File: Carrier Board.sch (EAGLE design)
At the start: 54 parts, among them J1 H4P-SMD-2.0, J2 H4P-SMD-2.0, J4 S2B-PH-SM4-TB(LF)(SN), J5 S2B-PH-SM4-TB(LF)(SN), Q1 MMBT2222A, SW2 MF-SW-TACT-6MM, U1 TMP36GRTZ, U2 TPL5010, U3 MB85RC64, U7 NAND

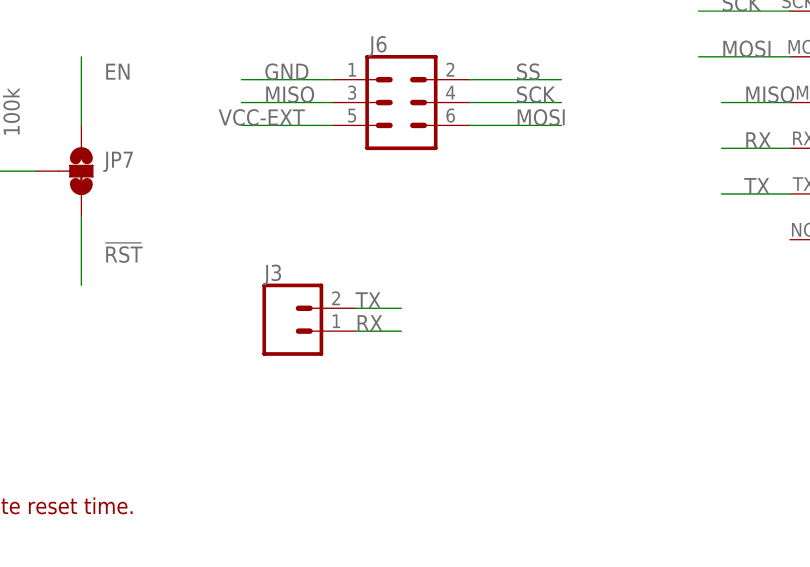
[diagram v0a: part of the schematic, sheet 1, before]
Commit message: v1.1 - Added a GND pin to serial
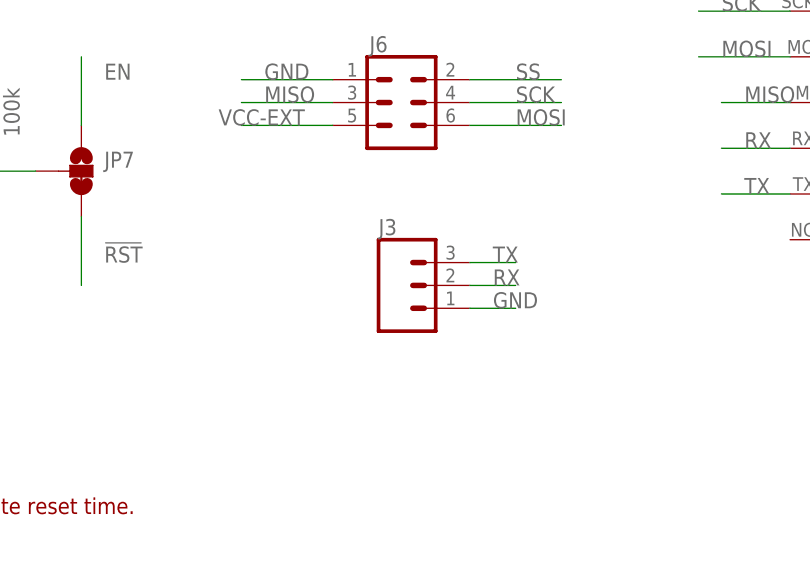
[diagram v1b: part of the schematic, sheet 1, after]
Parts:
- J3: device SparkFun-Connectors:CONN_02 -> SparkFun-Connectors:CONN_03LOCK
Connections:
- net GND: now also J3.1
- net RX: now also J3.2; no longer J3.1
- net TX: now also J3.3; no longer J3.2
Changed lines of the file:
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@@
 <part name="JP4" library="SparkFun" deviceset="STAND-OFF" device=""/>
 <part name="JP6" library="SparkFun" deviceset="STAND-OFF" device=""/>
-<part name="J3" library="SparkFun-Connectors" deviceset="CONN_02" device=""/>
 <part name="J5" library="SparkFun-Connectors" deviceset="JST_2MM_MALE" device="" value="S2B-PH-SM4-TB(LF)(SN)">
 <attribute name="MFG" value="S2B-PH-SM4-TB(LF)(SN)"/>
@@
 <part name="GND8" library="supply1" library_urn="urn:adsk.eagle:library:371" deviceset="GND" device=""/>
 <part name="J6" library="SparkFun-Connectors" library_urn="urn:adsk.eagle:library:513" deviceset="CONN_03X2" device="2X3_SILK_MALE_PTH" package3d_urn="urn:adsk.eagle:package:38016/1"/>
+<part name="J3" library="SparkFun-Connectors" library_urn="urn:adsk.eagle:library:513" deviceset="CONN_03" device="LOCK" package3d_urn="urn:adsk.eagle:package:38071/1"/>
 </parts>
 <sheets>
@@
 <instance part="JP4" gate="G$1" x="233.68" y="17.78" smashed="yes"/>
 <instance part="JP6" gate="G$1" x="243.84" y="17.78" smashed="yes"/>
-<instance part="J3" gate="G$1" x="101.6" y="81.28" smashed="yes">
-<attribute name="VALUE" x="99.06" y="76.454" size="1.778" layer="96" font="vector"/>
-<attribute name="NAME" x="99.06" y="86.868" size="1.778" layer="95" font="vector"/>
-</instance>
 <instance part="R3" gate="G$1" x="68.58" y="106.68" smashed="yes" rot="R90">
 <attribute name="NAME" x="67.0814" y="102.87" size="1.778" layer="95" rot="R90"/>
@@
 <attribute name="NAME" x="110.744" y="112.268" size="1.778" layer="95" font="vector"/>
 <attribute name="VALUE" x="110.998" y="100.838" size="1.778" layer="96" font="vector" align="top-left"/>
+</instance>
+<instance part="J3" gate="J$1" x="114.3" y="86.36" smashed="yes">
+<attribute name="VALUE" x="111.76" y="78.994" size="1.778" layer="96" font="vector"/>
+<attribute name="NAME" x="111.76" y="91.948" size="1.778" layer="95" font="vector"/>
 </instance>
 </instances>
@@
 <label x="99.06" y="109.22" size="1.778" layer="95"/>
 </segment>
+<segment>
+<wire x1="127" y1="83.82" x2="121.92" y2="83.82" width="0.1524" layer="91"/>
+<pinref part="J3" gate="J$1" pin="1"/>
+<label x="124.46" y="83.82" size="1.778" layer="95"/>
+</segment>
 </net>
 <net name="SCL" class="0">
@@
 <net name="TX" class="0">
 <segment>
-<pinref part="J3" gate="G$1" pin="2"/>
-<wire x1="109.22" y1="83.82" x2="114.3" y2="83.82" width="0.1524" layer="91"/>
-<label x="109.22" y="83.82" size="1.778" layer="95"/>
-</segment>
-<segment>
 <pinref part="BORON/ARGON/XENON" gate="G$1" pin="TX"/>
 <wire x1="157.48" y1="96.52" x2="149.86" y2="96.52" width="0.1524" layer="91"/>
 <label x="152.4" y="96.52" size="1.778" layer="95"/>
+</segment>
+<segment>
+<wire x1="121.92" y1="88.9" x2="127" y2="88.9" width="0.1524" layer="91"/>
+<pinref part="J3" gate="J$1" pin="3"/>
+<label x="124.46" y="88.9" size="1.778" layer="95"/>
 </segment>
 </net>
@@
 <net name="RX" class="0">
 <segment>
-<pinref part="J3" gate="G$1" pin="1"/>
-<wire x1="109.22" y1="81.28" x2="114.3" y2="81.28" width="0.1524" layer="91"/>
-<label x="109.22" y="81.28" size="1.778" layer="95"/>
-</segment>
-<segment>
 <pinref part="BORON/ARGON/XENON" gate="G$1" pin="RX"/>
 <wire x1="157.48" y1="101.6" x2="149.86" y2="101.6" width="0.1524" layer="91"/>
 <label x="152.4" y="101.6" size="1.778" layer="95"/>
 </segment>
-</net>
+<segment>
+<wire x1="121.92" y1="86.36" x2="127" y2="86.36" width="0.1524" layer="91"/>
+<pinref part="J3" gate="J$1" pin="2"/>
+<label x="124.46" y="86.36" size="1.778" layer="95"/>
+</segment>
+</net>

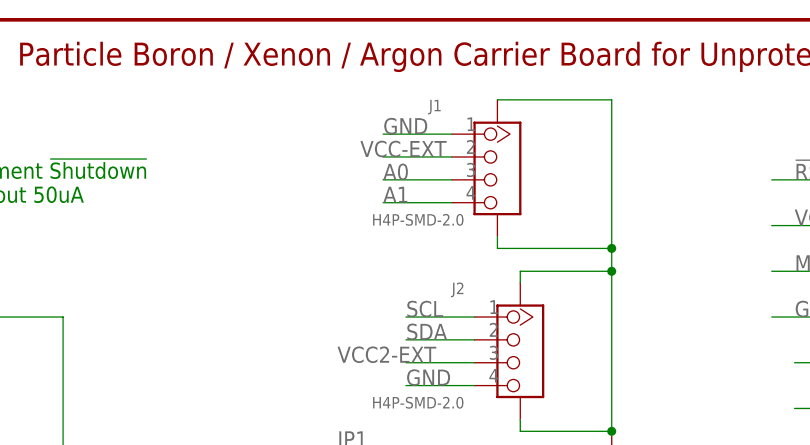
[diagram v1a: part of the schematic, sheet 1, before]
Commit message: Fixed Analoge Header Pins
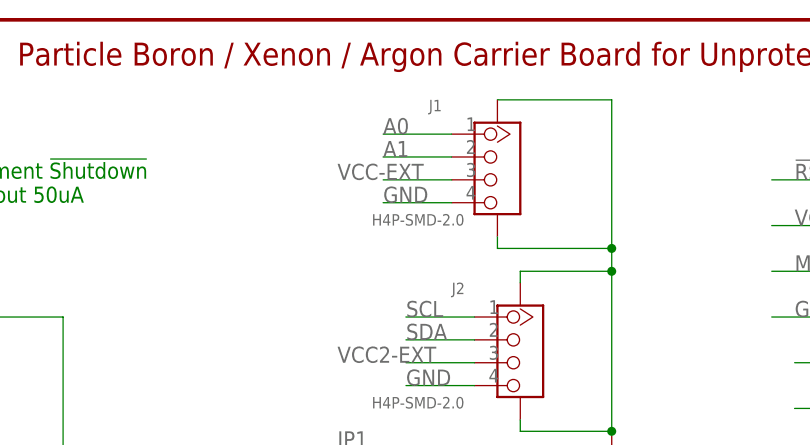
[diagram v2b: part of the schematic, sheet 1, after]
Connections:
- net A0: now also J1.1; no longer J1.3
- net A1: now also J1.2; no longer J1.4
- net GND: now also J1.4; no longer J1.1
- net VCC-EXT: now also J1.3; no longer J1.2
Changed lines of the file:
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@@
-</segment>
-<segment>
-<wire x1="104.14" y1="172.72" x2="111.76" y2="172.72" width="0.1524" layer="91"/>
-<label x="104.14" y="172.72" size="1.778" layer="95"/>
-<pinref part="J1" gate="G$1" pin="1"/>
 </segment>
 <segment>
@@
 <label x="124.46" y="83.82" size="1.778" layer="95"/>
 </segment>
+<segment>
+<wire x1="104.14" y1="165.1" x2="111.76" y2="165.1" width="0.1524" layer="91"/>
+<pinref part="J1" gate="G$1" pin="4"/>
+<label x="104.14" y="165.1" size="1.778" layer="95"/>
+</segment>
 </net>
 <net name="SCL" class="0">
@@
 <net name="VCC-EXT" class="0">
 <segment>
-<wire x1="104.14" y1="170.18" x2="111.76" y2="170.18" width="0.1524" layer="91"/>
-<pinref part="J1" gate="G$1" pin="2"/>
-<label x="101.6" y="170.18" size="1.778" layer="95"/>
-</segment>
-<segment>
 <pinref part="J6" gate="G$1" pin="5"/>
 <wire x1="106.68" y1="104.14" x2="96.52" y2="104.14" width="0.1524" layer="91"/>
 <label x="93.98" y="104.14" size="1.778" layer="95"/>
+</segment>
+<segment>
+<wire x1="104.14" y1="167.64" x2="111.76" y2="167.64" width="0.1524" layer="91"/>
+<pinref part="J1" gate="G$1" pin="3"/>
+<label x="99.06" y="167.64" size="1.778" layer="95"/>
 </segment>
 </net>
@@
 </segment>
 <segment>
-<wire x1="104.14" y1="167.64" x2="111.76" y2="167.64" width="0.1524" layer="91"/>
-<label x="104.14" y="167.64" size="1.778" layer="95"/>
-<pinref part="J1" gate="G$1" pin="3"/>
+<pinref part="J1" gate="G$1" pin="1"/>
+<wire x1="111.76" y1="172.72" x2="104.14" y2="172.72" width="0.1524" layer="91"/>
+<label x="104.14" y="172.72" size="1.778" layer="95"/>
 </segment>
 </net>
@@
 </segment>
 <segment>
-<wire x1="104.14" y1="165.1" x2="111.76" y2="165.1" width="0.1524" layer="91"/>
-<label x="104.14" y="165.1" size="1.778" layer="95"/>
-<pinref part="J1" gate="G$1" pin="4"/>
-</segment>
-</net>
+<pinref part="J1" gate="G$1" pin="2"/>
+<wire x1="111.76" y1="170.18" x2="104.14" y2="170.18" width="0.1524" layer="91"/>
+<label x="104.14" y="170.18" size="1.778" layer="95"/>
+</segment>
+</net>

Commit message: Next major revision - Added RTC
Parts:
- removed BORON/ARGON/XENON: PARTICLE-DEVICES-BORON, Carrier Board:PARTICLE-DEVICES-BORON
- removed D3: MF-DIO-SOD123-BAT42, MF_Discrete_Semiconductor:DIODES_BAT42_SOD-123
- removed JP7: JUMPER-SMT_3_1-NC_TRACE_SILK, SparkFun-Jumpers:JUMPER-SMT_3_1-NC_TRACE_SILK
- removed JP9: JUMPER-SMT_2_NC_PASTE_SILK, SparkFun-Jumpers:JUMPER-SMT_2_NC_PASTE_SILK
- removed R10: 10k, SparkFun-Passives:RESISTOR0805-RES
- removed R11, R13, R14: 100k, SparkFun-Passives:RESISTOR0805-RES
- removed R12: 100, SparkFun-Passives:RESISTOR0805-RES
- removed S2: B3F-4000, adafruit:40-XX-ROUND
- removed SW2: MF-SW-TACT-6MM, MF_Switches:TACT_6MM
- added C11: 10pF, SparkFun-Capacitors:CAP0805
- added C12: 8.2pF, SparkFun-Capacitors:CAP0805
- added C6, C7: 0.1uF, SparkFun-Capacitors:CAP0805
- added H1, H2, H3, H4: STAND-OFF-M2.5, Custom Components:STAND-OFF-M2.5
- added JP2: (no value), SparkFun-Connectors:M06LOCK
- added P1: PARTICLE-DEVICES-BORON, Carrier Board:PARTICLE-DEVICES-BORON
- added Q2: BSS138, transistor-small-signal:BSS123
- added R20, R21, R22: 10k, SparkFun-Passives:RESISTOR0805-RES
- added R8, R9: 100, SparkFun-Passives:RESISTOR0805-RES
- added S1: (no value), SparkFun-Switches:SWITCH-SPDT-SMD-AYZ0202
- added SW1: MF-SW-TACT-6MM, MF_Switches:TACT_6MM
- added U4, U5: TPS22810, Custom Components:TPS22810
- added U8: MCP79410T-I/SN, Custom Components:MCP79410T-I/SN
- added Y1: ECS-.327-6-17X-TR, Custom Components:ECS-.327-6-17X-TR
- C1: HOUSEPART (none) -> YES; MPN (none) -> MF-CAP-0805-0.1uF; POPULATE (none) -> 1
- C2: MPN (none) -> MF-CAP-0805-1uF
- C3: MPN (none) -> MF-CAP-0805-0.1uF; POPULATE (none) -> 1
- C4: value 0.1uF -> 10nF; HOUSEPART (none) -> No; MPN (none) -> 08051C103K4T2A; POPULATE (none) -> 1
- C5: value 1uF -> 10nF; HOUSEPART (none) -> No; MPN (none) -> 08051C103K4T2A; POPULATE (none) -> 1
- C8: HOUSEPART (none) -> 1; MPN (none) -> MF-CAP-10MM-470uF
- D1, D2: value MF-DIO-SOD123-BAT42 -> BAT42
- F1: value 1.5A - SLOW BLOW -> 6V/0.5A; MPN (none) -> 046801.5NR
- F2, F3: value 500mA - FAST BLOW -> 6V/0.5A; MPN (none) -> 0466.500NR
- FD1, FD2, FRAME1, FRAME2, FRAME3: POPULATE (none) -> 0
- G1: MPN (none) -> D5V0L4B5TS-7
- J1, J2: MPN (none) -> B4B-PH-SM4-TB(LF)(SN); POPULATE (none) -> 1
- J3: value (none) -> H4P-SMD-2.0; device SparkFun-Connectors:CONN_03LOCK -> OPL_Connector:GROVE-CONNECTOR-SMD(4+2P-2.0); MPN (none) -> B4B-PH-SM4-TB(LF)(SN); POPULATE (none) -> 1
- J4: value S2B-PH-SM4-TB(LF)(SN) -> (none); device SparkFun-Connectors:JST_2MM_MALE -> SparkFun-Connectors:CONN_03X22X3_SILK_MALE_PTH; MFG S2B-PH-SM4-TB(LF)(SN) -> (none); POPULATE (none) -> 0
- J5: MFG S2B-PH-SM4-TB(LF)(SN) -> JST S2B-PH-SM4-TB(LF)(SN)
- J6: value (none) -> S2B-PH-SM4-TB(LF)(SN); device SparkFun-Connectors:CONN_03X22X3_SILK_MALE_PTH -> SparkFun-Connectors:JST_2MM_MALE; MFG (none) -> JST S2B-PH-SM4-TB(LF)(SN)
- JP1: value (none) -> JUMPER-SMT_2_NC_PASTE_SILK; device SparkFun-Connectors:M06LOCK -> SparkFun-Jumpers:JUMPER-SMT_2_NC_PASTE_SILK; POPULATE (none) -> 0
- JP3, JP4, JP5, JP6: device SparkFun:STAND-OFF -> SparkFun-Hardware:STAND-OFF; POPULATE (none) -> 0
- Q1: value MMBT2222A -> BSS138; device SparkFun-DiscreteSemi:TRANS_NPN-MMBT2222AL -> transistor-small-signal:BSS123; HOUSEPART (none) -> Yes; MPN (none) -> MF-DSC-SOT233-BSS138
- R1, R2: MPN (none) -> ERJ-P06F2703V
- R3: HOUSEPART (none) -> YES; MPN (none) -> MF-RES-0805-100K
- R4: value 100k -> 4.7k; MPN (none) -> MF-RES-0805-4.7K
- R5: value 10k -> 4.7k; MPN (none) -> MF-RES-0805-4.7K
- R6: value 4.7k -> 100k; HOUSEPART (none) -> YES; MPN (none) -> MF-RES-0805-100K
- R7: value 4.7k -> 10k; HOUSEPART (none) -> YES; MPN (none) -> MF-RES-0805-10K
- U1: MANUFACTURER_PART_NUMBER (none) -> TMP36GRTZ-REEL7; MPN (none) -> TMP36GRTZ-REEL7
- U2: value TPL5010 -> MB85RC64; device Custom Components:TPL5010 -> Fujitsu_By_element14_Batch_1:MB85RC128PNF-G-JNE1; MPN (none) -> MB85RC64PNF-G-JNE1
- U3: value MB85RC64 -> TPL5010; device Fujitsu_By_element14_Batch_1:MB85RC128PNF-G-JNE1 -> Custom Components:TPL5010; MPN (none) -> TPL5010DDCR; POPULATE (none) -> 1
- U7: value NAND -> NL17SZ74USG; device adafruit:4093DT -> Custom Components:NL17SZ74USG
- V1, V2, V3: MPN (none) -> VC080505C150DP
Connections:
- removed net !HARD-RESET: C5.1, D1.ANODE, R12.1, R14.1, U7B.I1
- removed net BUTTON-STATE: R13.1, U7B.I0, U7D.O
- removed net DC-IN-EXT: F1.1, J4.+
- removed net ENABLE-PWR: D1.CATHODE, D2.CATHODE, D3.CATHODE, R14.2, U7P.VDD
- removed net HARD-RESET: BORON/ARGON/XENON.D6, R10.2
- removed net N$1: U7A.I0, U7A.I1, U7B.O
- removed net N$19: Q1.C, R12.2
- removed net N$24: C4.1, R11.2, S2.P, S2.P1
- removed net N$25: R13.2, S2.S, S2.S1, U7C.I0, U7C.I1
- removed net RESET: JP7.2, R3.1, U2.!RST
- new net BATT-IN: D1.ANODE, J5.+, U4.VIN, U8.VBAT
- new net DEEP-SLEEP: P1.D6, Q1.G, R20.2
- new net EN/UVLO: C4.1, C5.1, S1.P, U4.EN/UVLO, U5.EN/UVLO
- new net N$10: C7.1, U4.CT
- new net N$11: D2.ANODE, J6.+, U5.VIN
- new net N$12: R9.1, U4.QOD
- new net N$13: Q2.G, U7.~Q
- new net N$15: C12.1, U8.X1, Y1.1
- new net N$2: P1.D5
- new net N$5: C6.1, U5.CT
- new net N$6: R8.1, U5.QOD
- new net N$7: F1.1, R8.2, U5.VOUT
- new net N$9: D1.CATHODE, D2.CATHODE, S1.S
- new net RTC-INT: R22.1, U7.~PR, U8.MFP
- net !RST: now also P1.!RST, R3.1, U3.!RST; no longer BORON/ARGON/XENON.!RST, JP7.3
- net A0: now also P1.A0; no longer BORON/ARGON/XENON.A0
- net A1: now also P1.A1; no longer BORON/ARGON/XENON.A1
- net A2: now also P1.A2; no longer BORON/ARGON/XENON.A2
- net D2: now also JP2.3, P1.D2; no longer BORON/ARGON/XENON.D2, JP1.3
- net D3: now also JP2.2, P1.D3; no longer BORON/ARGON/XENON.D3, JP1.2
- net DELAY: now also U3.DELAY; no longer U2.DELAY
- net DONE: now also P1.A3, U3.DONE; no longer BORON/ARGON/XENON.A3, U2.DONE
- net EN: now also P1.EN, Q2.D; no longer BORON/ARGON/XENON.EN, JP7.1, U7A.O
- net GND: now also C11.2, C12.2, C6.2, C7.2, J3.4, J3.SS1, J3.SS2, J4.1, J6.-, JP2.1, P1.GND, Q1.S, Q2.S, R20.1, S1.O, SW1.P$3, SW1.P$4, U2.A0, U2.A1, U2.A2, U2.VSS, U2.WP, U3.GND, U4.GND, U5.GND, U7.CP, U7.D, U7.GND, U8.VSS, Y1.2, Y1.3; no longer BORON/ARGON/XENON.GND, J3.1, J4.-, J6.1, JP1.1, Q1.E, SW2.P$3, SW2.P$4, U2.GND, U3.A0, U3.A1, U3.A2, U3.VSS, U3.WP, U7P.VSS
- net LI+: now also P1.LI+, R21.2, R22.2, R9.2, U4.VOUT, U7.VCC; no longer BORON/ARGON/XENON.LI+, D2.ANODE, J5.+
- net MD: now also P1.MD; no longer BORON/ARGON/XENON.MD
- net MISO: now also J4.3, P1.MI; no longer BORON/ARGON/XENON.MI, J6.3
- net MOSI: now also J4.6, P1.MO; no longer BORON/ARGON/XENON.MO, J6.6
- net N$14: now also Q1.D, R21.1, U7.~CLR; no longer R11.1, U7C.O, U7D.I0, U7D.I1
- net N$16: now also C11.1, U8.X2, Y1.4; no longer Q1.B, R10.1
- net N$4: now also R6.1, R7.2, SW1.P$1, SW1.P$2; no longer R4.1, R5.2, SW2.P$1, SW2.P$2
- net RX: now also J3.1, P1.RX; no longer BORON/ARGON/XENON.RX, J3.2
- net SCK: now also J4.4, P1.SCK; no longer BORON/ARGON/XENON.SCK, J6.4
- net SCL: now also JP2.4, P1.SCL, R5.1, U2.SCL, U8.SCL; no longer BORON/ARGON/XENON.SCL, JP1.4, R7.1, U3.SCL
- net SDA: now also JP2.5, P1.SDA, R4.1, U2.SDA, U8.SDA; no longer BORON/ARGON/XENON.SDA, JP1.5, R6.1, U3.SDA
- net SS: now also J4.2, P1.A5; no longer BORON/ARGON/XENON.A5, J6.2
- net TEMP: now also P1.A4; no longer BORON/ARGON/XENON.A4
- net TX: now also J3.2, P1.TX; no longer BORON/ARGON/XENON.TX, J3.3
- net USER-SW: now also P1.D4, R7.1; no longer BORON/ARGON/XENON.D4, R5.1
- net VCC: now also JP1.2, P1.3V3, R5.2, U2.VDD, U8.VCC; no longer BORON/ARGON/XENON.3V3, JP9.2, R7.2, U3.VDD
- net VCC-EXT: now also J3.3, J4.5; no longer J6.5
- net VCC2-EXT: now also JP2.6; no longer JP1.6
- net VDD: now also JP1.1, U3.VDD; no longer JP9.1, U2.VDD
- net VUSB: now also P1.VUSB; no longer BORON/ARGON/XENON.VUSB, D3.ANODE
- net WAKE: now also P1.D8, U3.WAKE; no longer BORON/ARGON/XENON.D8, U2.WAKE
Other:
- note added: "Operating Instructions: BATT-IN is on whenever a battery is connected Li+ is on when there is a battery and when the switch SW1 is on. Note, RTC functionality is available for applications with no battery but not the control over the EN pin. D6 / DEEP SLEEP on the Electron can put the device into deep sleep and then only the RTC can wake it."
- note added: "Operating Instructions: SW1 - Connects / disconnects power for long term storage and transport. Only RTC VBatt runs when the switch is off. SW1 - Enables the two power switches and is powered by either Battery or DC-In RTC Power will be the higher or Li+ or DC-In"
- note added: "Particle Boron / Argon / Xenon Carrier Board"
- note added: "Particle Boron / Argon / Xenon Carrier Board - Real Time Clock"
- note added: "v1.1"
- note removed: "!HARD-RESET !connected to D5. HIGH will cut power for 100mSec."
- note removed: "4093 QUAD NAND"
- note removed: "Logic Table: If Button-State is HIGH AND HARD-RST is LOW then power is ON If Button-State is LOW AND Hard-RST is LOW then power is OFF if Button-State ON AND Hard-RST is HIGH then power is OFF"
- note removed: "Particle Boron / Xenon / Argon Carrier Board - Power Protection"
- note removed: "Power Control - Push Button and !Hard-Reset"
- note removed: "Protection Circuits for External Connections"
- note removed: "Ran out of pins so will not implement !Shutdown on the TMP-36. It draws only about 50uA"
- note removed: "S1 is a momentary On switch. Pressing will cycle power."
- note removed: "This change enables operation w/o the LiPo battery"
- note removed: "v1.0"
